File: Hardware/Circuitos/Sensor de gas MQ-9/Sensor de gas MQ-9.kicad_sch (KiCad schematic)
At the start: 3 parts, among them J1 Conn_01x04

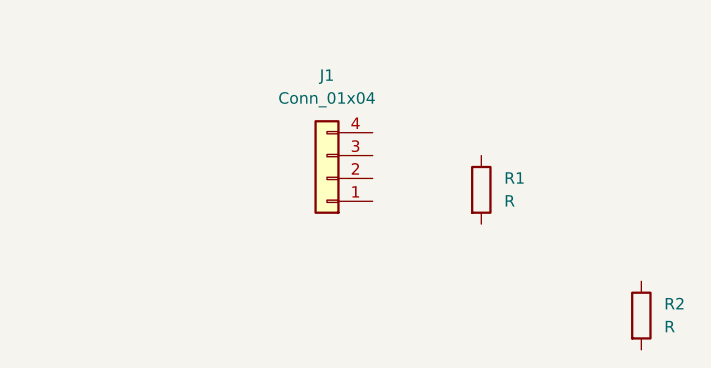
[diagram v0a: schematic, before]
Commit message: Placa MQ9 - Colocar MQ-9
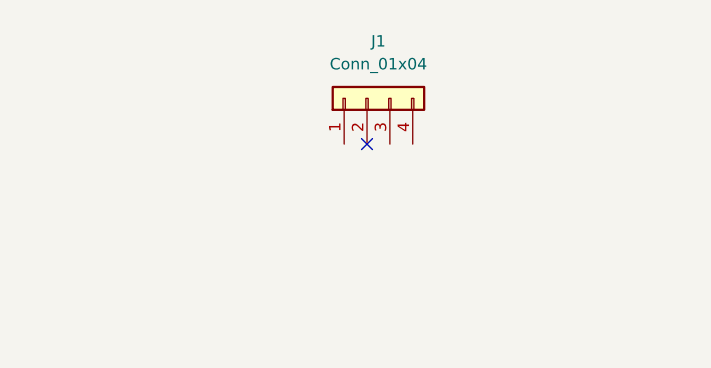
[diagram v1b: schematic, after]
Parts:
- removed R1, R2: R, symbol Device:R
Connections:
- no-connect marks 0 -> 1
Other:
- moved on the sheet: J1
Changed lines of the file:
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@@
 	(generator_version "10.0")
 	(paper "A4")
+	(no_connect
+		(at 96.52 54.61)
+	)
 	(symbol
 		(lib_id "Connector_Generic:Conn_01x04")
-		(at 92.075 58.42 180)
+		(at 96.52 49.53 90)
 		(unit 1)
 		(body_style 1)
@@
 		(fields_autoplaced yes)
 		(property "Reference" "J1"
-			(at 92.075 46.99 0)
+			(at 97.79 43.18 90)
 			(show_name no)
 			(do_not_autoplace no)
@@
 		)
 		(property "Value" "Conn_01x04"
-			(at 92.075 49.53 0)
+			(at 97.79 45.72 90)
 			(show_name no)
 			(do_not_autoplace no)
@@
 		)
 		(property "Footprint" ""
-			(at 92.075 58.42 0)
+			(at 96.52 49.53 0)
 			(hide yes)
 			(show_name no)
@@
 		)
 		(property "Datasheet" ""
-			(at 92.075 58.42 0)
+			(at 96.52 49.53 0)
 			(hide yes)
 			(show_name no)
@@
 		)
 		(property "Description" "Generic connector, single row, 01x04, script generated (kicad-library-utils/schlib/autogen/connector/)"
-			(at 92.075 58.42 0)
+			(at 96.52 49.53 0)
 			(hide yes)
 			(show_name no)
@@
 					(unit 1)
 				)
-			)
-		)
-	)
-	(symbol
-		(lib_id "Device:R")
-		(at 109.22 59.69 0)
-		(unit 1)
-		(body_style 1)
-		(exclude_from_sim no)
-		(in_bom yes)
-		(on_board yes)
-		(in_pos_files yes)
-		(dnp no)
-		(fields_autoplaced yes)
-		(property "Reference" "R1"
-			(at 111.76 58.4199 0)
-			(show_name no)
-			(do_not_autoplace no)
-			(effects
-				(font
-					(size 1.27 1.27)
-				)
-				(justify left)
-			)
-		)
-		(property "Value" "R"
-			(at 111.76 60.9599 0)
-			(show_name no)
-			(do_not_autoplace no)
-			(effects
-				(font
-					(size 1.27 1.27)
-				)
-				(justify left)
-			)
-		)
-		(property "Footprint" ""
-			(at 107.442 59.69 90)
-			(hide yes)
-			(show_name no)
-			(do_not_autoplace no)
-			(effects
-				(font
-					(size 1.27 1.27)
-				)
-			)
-		)
-		(property "Datasheet" ""
-			(at 109.22 59.69 0)
-			(hide yes)
-			(show_name no)
-			(do_not_autoplace no)
-			(effects
-				(font
-					(size 1.27 1.27)
-				)
-			)
-		)
-		(property "Description" "Resistor"
-			(at 109.22 59.69 0)
-			(hide yes)
-			(show_name no)
-			(do_not_autoplace no)
-			(effects
-				(font
-					(size 1.27 1.27)
-				)
-			)
-		)
-		(pin "1"
-		)
-		(pin "2"
-		)
-		(instances
-			(project "Sensor de gas MQ-9"
-				(path "/3bed7055-d8f6-45bf-9b4e-d6a9d47d2179"
-					(reference "R1")
-					(unit 1)
-				)
-			)
-		)
-	)
-	(symbol
-		(lib_id "Device:R")
-		(at 127 73.66 0)
-		(unit 1)
-		(body_style 1)
-		(exclude_from_sim no)
-		(in_bom yes)
-		(on_board yes)
-		(in_pos_files yes)
-		(dnp no)
-		(fields_autoplaced yes)
-		(property "Reference" "R2"
-			(at 129.54 72.3899 0)
-			(show_name no)
-			(do_not_autoplace no)
-			(effects
-				(font
-					(size 1.27 1.27)
-				)
-				(justify left)
-			)
-		)
-		(property "Value" "R"
-			(at 129.54 74.9299 0)
-			(show_name no)
-			(do_not_autoplace no)
-			(effects
-				(font
-					(size 1.27 1.27)
-				)
-				(justify left)
-			)
-		)
-		(property "Footprint" ""
-			(at 125.222 73.66 90)
-			(hide yes)
-			(show_name no)
-			(do_not_autoplace no)
-			(effects
-				(font
-					(size 1.27 1.27)
-				)
-			)
-		)
-		(property "Datasheet" ""
-			(at 127 73.66 0)
-			(hide yes)
-			(show_name no)
-			(do_not_autoplace no)
-			(effects
-				(font
-					(size 1.27 1.27)
-				)
-			)
-		)
-		(property "Description" "Resistor"
-			(at 127 73.66 0)
-			(hide yes)
-			(show_name no)
-			(do_not_autoplace no)
-			(effects
-				(font
-					(size 1.27 1.27)
-				)
-			)
-		)
-		(pin "1"
-		)
-		(pin "2"
-		)
-		(instances
-			(project "Sensor de gas MQ-9"
-				(path "/3bed7055-d8f6-45bf-9b4e-d6a9d47d2179"
-					(reference "R2")
-					(unit 1)
-				)

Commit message: Placa MQ9 - Divisor de tension y IN 5V
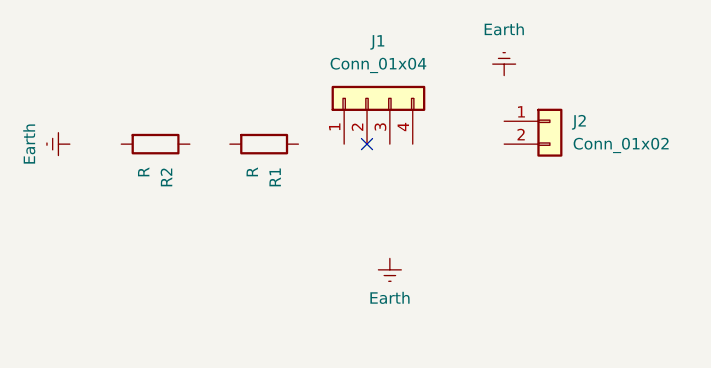
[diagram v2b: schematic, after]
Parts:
- added J2: Conn_01x02, symbol Connector_Generic:Conn_01x02
- added R1, R2: R, symbol Device:R

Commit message: Placa MQ9 - Conexión
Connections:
- net Earth: now also J1.3 (Pin_3), J2.1 (Pin_1), R2.2
- net at J1.1 (Pin_1): now also R1.1
- net at J1.4 (Pin_4): now also J2.2 (Pin_2)
- net at R1.2: now also R2.1
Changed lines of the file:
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@@
 		(at 96.52 54.61)
+	)
+	(wire
+		(pts
+			(xy 101.6 54.61) (xy 111.76 54.61)
+		)
+		(stroke
+			(width 0)
+			(type default)
+		)
+	)
+	(wire
+		(pts
+			(xy 111.76 46.99) (xy 111.76 52.07)
+		)
+		(stroke
+			(width 0)
+			(type default)
+		)
+	)
+	(wire
+		(pts
+			(xy 88.9 54.61) (xy 93.98 54.61)
+		)
+		(stroke
+			(width 0)
+			(type default)
+		)
+	)
+	(wire
+		(pts
+			(xy 76.835 54.61) (xy 81.28 54.61)
+		)
+		(stroke
+			(width 0)
+			(type default)
+		)
+	)
+	(wire
+		(pts
+			(xy 99.06 67.31) (xy 99.06 54.61)
+		)
+		(stroke
+			(width 0)
+			(type default)
+		)
+	)
+	(wire
+		(pts
+			(xy 63.5 54.61) (xy 69.215 54.61)
+		)
+		(stroke
+			(width 0)
+			(type default)
+		)
 	)
 	(symbol

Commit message: Placa MQ9 - Colocar OUT a ESP32
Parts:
- added J3: Conn_01x01, symbol Connector_Generic:Conn_01x01
- J1: footprint (none) -> Connector_PinHeader_2.54mm:PinHeader_1x04_P2.54mm_Vertical
- J2: footprint (none) -> Connector_PinHeader_2.54mm:PinHeader_1x02_P2.54mm_Vertical
- R1, R2: footprint (none) -> Resistor_THT:R_Axial_DIN0411_L9.9mm_D3.6mm_P15.24mm_Horizontal
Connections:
- net at R1.2, R2.1: now also J3.1 (Pin_1)
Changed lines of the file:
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@@
 	(generator_version "10.0")
 	(paper "A4")
+	(junction
+		(at 79.375 54.61)
+		(diameter 0)
+		(color 0 0 0 0)
+	)
 	(no_connect
 		(at 96.52 54.61)
@@
 	(wire
 		(pts
+			(xy 79.375 54.61) (xy 81.28 54.61)
+		)
+		(stroke
+			(width 0)
+			(type default)
+		)
+	)
+	(wire
+		(pts
 			(xy 111.76 46.99) (xy 111.76 52.07)
 		)
@@
 	(wire
 		(pts
-			(xy 76.835 54.61) (xy 81.28 54.61)
+			(xy 76.835 54.61) (xy 79.375 54.61)
 		)
 		(stroke
@@
 		(pts
 			(xy 63.5 54.61) (xy 69.215 54.61)
+		)
+		(stroke
+			(width 0)
+			(type default)
+		)
+	)
+	(wire
+		(pts
+			(xy 79.375 54.61) (xy 79.375 63.5)
 		)
 		(stroke
@@
 			)
 		)
-		(property "Footprint" ""
+		(property "Footprint" "Connector_PinHeader_2.54mm:PinHeader_1x04_P2.54mm_Vertical"
 			(at 96.52 49.53 0)
 			(hide yes)
@@
 			)
 		)
-		(property "Footprint" ""
+		(property "Footprint" "Connector_PinHeader_2.54mm:PinHeader_1x02_P2.54mm_Vertical"
 			(at 116.84 52.07 0)
 			(hide yes)
@@
 			)
 		)
-		(property "Footprint" ""
+		(property "Footprint" "Resistor_THT:R_Axial_DIN0411_L9.9mm_D3.6mm_P15.24mm_Horizontal"
 			(at 85.09 52.832 90)
 			(hide yes)
@@
 	)
 	(symbol
+		(lib_id "Connector_Generic:Conn_01x01")
+		(at 79.375 68.58 270)
+		(unit 1)
+		(body_style 1)
+		(exclude_from_sim no)
+		(in_bom yes)
+		(on_board yes)
+		(in_pos_files yes)
+		(dnp no)
+		(fields_autoplaced yes)
+		(property "Reference" "J3"
+			(at 82.55 67.3099 90)
+			(show_name no)
+			(do_not_autoplace no)
+			(effects
+				(font
+					(size 1.27 1.27)
+				)
+				(justify left)
+			)
+		)
+		(property "Value" "Conn_01x01"
+			(at 82.55 69.8499 90)
+			(show_name no)
+			(do_not_autoplace no)
+			(effects
+				(font
+					(size 1.27 1.27)
+				)
+				(justify left)
+			)
+		)
+		(property "Footprint" ""
+			(at 79.375 68.58 0)
+			(hide yes)
+			(show_name no)
+			(do_not_autoplace no)
+			(effects
+				(font
+					(size 1.27 1.27)
+				)
+			)
+		)
+		(property "Datasheet" ""
+			(at 79.375 68.58 0)
+			(hide yes)
+			(show_name no)
+			(do_not_autoplace no)
+			(effects
+				(font
+					(size 1.27 1.27)
+				)
+			)
+		)
+		(property "Description" "Generic connector, single row, 01x01, script generated (kicad-library-utils/schlib/autogen/connector/)"
+			(at 79.375 68.58 0)
+			(hide yes)
+			(show_name no)
+			(do_not_autoplace no)
+			(effects
+				(font
+					(size 1.27 1.27)
+				)
+			)
+		)
+		(pin "1"
+		)
+		(instances
+			(project "Sensor de gas MQ-9"
+				(path "/3bed7055-d8f6-45bf-9b4e-d6a9d47d2179"
+					(reference "J3")
+					(unit 1)
+				)
+			)
+		)
+	)
+	(symbol
 		(lib_id "Device:R")
 		(at 73.025 54.61 270)
@@
 			)
 		)
-		(property "Footprint" ""
+		(property "Footprint" "Resistor_THT:R_Axial_DIN0411_L9.9mm_D3.6mm_P15.24mm_Horizontal"
 			(at 73.025 52.832 90)
 			(hide yes)

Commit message: Placa MQ9 - Asignación de huellas
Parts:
- J3: footprint (none) -> Connector_PinHeader_2.00mm:PinHeader_1x01_P2.00mm_Vertical
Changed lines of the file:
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@@
 			)
 		)
-		(property "Footprint" ""
+		(property "Footprint" "Connector_PinHeader_2.00mm:PinHeader_1x01_P2.00mm_Vertical"
 			(at 79.375 68.58 0)
 			(hide yes)

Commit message: Placa MQ9 - Corrección de huella
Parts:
- J2: footprint Connector_PinHeader_2.54mm:PinHeader_1x02_P2.54mm_Vertical -> Connector_Molex:Molex_KK-254_AE-6410-02A_1x02_P2.54mm_Vertical
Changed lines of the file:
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@@
 			)
 		)
-		(property "Footprint" "Connector_PinHeader_2.54mm:PinHeader_1x02_P2.54mm_Vertical"
+		(property "Footprint" "Connector_Molex:Molex_KK-254_AE-6410-02A_1x02_P2.54mm_Vertical"
 			(at 116.84 52.07 0)
 			(hide yes)

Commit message: Placa MQ9 - Colocación de componentes
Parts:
- R1, R2: footprint Resistor_THT:R_Axial_DIN0411_L9.9mm_D3.6mm_P15.24mm_Horizontal -> Resistor_THT:R_Axial_DIN0207_L6.3mm_D2.5mm_P7.62mm_Horizontal
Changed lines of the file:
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@@
 			)
 		)
-		(property "Footprint" "Resistor_THT:R_Axial_DIN0411_L9.9mm_D3.6mm_P15.24mm_Horizontal"
+		(property "Footprint" "Resistor_THT:R_Axial_DIN0207_L6.3mm_D2.5mm_P7.62mm_Horizontal"
 			(at 85.09 52.832 90)
 			(hide yes)
@@
 			)
 		)
-		(property "Footprint" "Resistor_THT:R_Axial_DIN0411_L9.9mm_D3.6mm_P15.24mm_Horizontal"
+		(property "Footprint" "Resistor_THT:R_Axial_DIN0207_L6.3mm_D2.5mm_P7.62mm_Horizontal"
 			(at 73.025 52.832 90)
 			(hide yes)
